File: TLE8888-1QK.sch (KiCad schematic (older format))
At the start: 38 parts, among them Q1 IPD30N06S2L-23, U2 TLE8888QK

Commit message: Update (#46)
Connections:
- net CRNK+: now also R17.2
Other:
- moved on the sheet: R17
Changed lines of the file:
@@
 L Device:R R17
 U 1 1 5C8A0B54
-P 11425 5850
-F 0 "R17" V 11475 6025 50  0000 C CNN
-F 1 "DNP" V 11425 5850 50  0000 C CNN
-F 2 "Resistor_SMD:R_0603_1608Metric_Pad1.05x0.95mm_HandSolder" V 11355 5850 50  0001 C CNN
-F 3 "~" H 11425 5850 50  0001 C CNN
-F 4 "MOUSER" H -3025 -500 50  0001 C CNN "VEND"
-	1    11425 5850
+P 13075 5900
+F 0 "R17" V 13125 6075 50  0000 C CNN
+F 1 "DNP" V 13075 5900 50  0000 C CNN
+F 2 "Resistor_SMD:R_0603_1608Metric_Pad1.05x0.95mm_HandSolder" V 13005 5900 50  0001 C CNN
+F 3 "~" H 13075 5900 50  0001 C CNN
+F 4 "MOUSER" H -1375 -450 50  0001 C CNN "VEND"
+	1    13075 5900
 	0    1    1    0
 $EndComp
@@
 Wire Wire Line
 	9750 10725 9750 11200
-Text Label 11900 11300 3    60   ~ 0
+Text Label 11900 11300 3    60   ~ 6
 VDD
-Text HLabel 11900 11200 2    60   Input ~ 0
+Text HLabel 11900 11200 2    60   Input ~ 6
 VDD
 Wire Wire Line
@@
 Wire Wire Line
 	11900 10500 11900 10800
-Text Label 12850 10300 0    60   ~ 0
+Text Label 12850 10300 0    60   ~ 6
 VDD
-Text Label 7200 10700 2    60   ~ 0
+Text Label 7200 10700 2    60   ~ 6
 VDD
 Wire Wire Line
 	7500 10700 9250 10700
-Text Label 7300 10100 2    60   ~ 0
+Text Label 7300 10100 2    60   ~ 6
 VDD
 Wire Wire Line
@@
 Connection ~ 12850 6550
 Wire Wire Line
-	11275 5900 11075 5900
-Wire Wire Line
-	11275 5900 11275 5850
+	12925 5950 12725 5950
+Wire Wire Line
+	12925 5950 12925 5900
 Wire Wire Line
 	13000 6800 13050 6800
@@
 	11150 6500 11150 6450
 Wire Wire Line
-	11075 5900 11075 6200
+	12725 5950 12725 6250
 Wire Wire Line
 	12850 6550 12850 6750
@@
 Wire Notes Line
 	14500 7000 14500 5650
-Text Notes 13750 6050 0    50   ~ 0
+Text Notes 13750 6050 0    50   ~ 6
 TRIGGER CONFIG\nAS SEEN\nAT PCB
 Text Label 13475 6800 0    60   ~ 12
@@
 Text Label 13475 6700 0    60   ~ 12
 GND
-Text Label 11575 5850 0    60   ~ 12
+Text Label 13225 5900 0    60   ~ 12
 V5V
 Text Label 13675 7150 0    60   ~ 12
@@
 	1    0    0    -1
 $EndComp
-Text Notes 13575 6450 0    50   ~ 0
+Text Notes 13575 6450 0    50   ~ 6
 SEE DATASHEET \nFOR HALL SENSOR USE
 Wire Wire Line
@@
 Connection ~ 12675 6250
 Wire Wire Line
-	12675 6250 12800 6250
+	12675 6250 12725 6250
 Connection ~ 12675 6550
 Wire Wire Line
@@
 Wire Wire Line
 	12800 6250 13175 6250
+Connection ~ 12725 6250
+Wire Wire Line
+	12725 6250 12800 6250
 $EndSCHEMATC

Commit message: Ready To Go! (#53)
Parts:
- R12, R13, R17, R18, R19, R20, R21: VEND MOUSER -> (none)
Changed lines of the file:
@@
 F 2 "Resistor_SMD:R_0603_1608Metric_Pad1.05x0.95mm_HandSolder" V 12380 6250 50  0001 C CNN
 F 3 "~" H 12450 6250 50  0001 C CNN
-F 4 "MOUSER" H -2000 -250 50  0001 C CNN "VEND"
 	1    12450 6250
 	0    1    1    0
@@
 F 2 "Resistor_SMD:R_0603_1608Metric_Pad1.05x0.95mm_HandSolder" V 12380 6550 50  0001 C CNN
 F 3 "~" H 12450 6550 50  0001 C CNN
-F 4 "MOUSER" H -2000 -250 50  0001 C CNN "VEND"
 	1    12450 6550
 	0    1    1    0
@@
 F 2 "Resistor_SMD:R_0603_1608Metric_Pad1.05x0.95mm_HandSolder" V 13005 5900 50  0001 C CNN
 F 3 "~" H 13075 5900 50  0001 C CNN
-F 4 "MOUSER" H -1375 -450 50  0001 C CNN "VEND"
 	1    13075 5900
 	0    1    1    0
@@
 F 2 "Resistor_SMD:R_0603_1608Metric_Pad1.05x0.95mm_HandSolder" V 12730 7300 50  0001 C CNN
 F 3 "~" H 12800 7300 50  0001 C CNN
-F 4 "MOUSER" H -1250 1900 50  0001 C CNN "VEND"
 	1    12800 7300
 	1    0    0    1
@@
 F 2 "Resistor_SMD:R_0603_1608Metric_Pad1.05x0.95mm_HandSolder" V 13255 7150 50  0001 C CNN
 F 3 "~" H 13325 7150 50  0001 C CNN
-F 4 "MOUSER" H -925 1900 50  0001 C CNN "VEND"
 	1    13325 7150
 	0    -1   1    0
@@
 F 2 "Resistor_SMD:R_0603_1608Metric_Pad1.05x0.95mm_HandSolder" V 13130 6700 50  0001 C CNN
 F 3 "~" H 13200 6700 50  0001 C CNN
-F 4 "MOUSER" H -1250 -250 50  0001 C CNN "VEND"
 	1    13200 6700
 	0    1    1    0
@@
 F 2 "Resistor_SMD:R_0603_1608Metric_Pad1.05x0.95mm_HandSolder" V 13130 6800 50  0001 C CNN
 F 3 "~" H 13200 6800 50  0001 C CNN
-F 4 "MOUSER" H -1250 -150 50  0001 C CNN "VEND"
 	1    13200 6800
 	0    1    1    0

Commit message: Mostly Ola's e-mailed copy, plus some of my own fixes to his almost done revision. I also did some house cleaning, with boundary edges, removed most DRC and ERC errors, etc.
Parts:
- C1, C10, C11, C12, C13, C14, C16, C3, C35, C4, C5, C6, C7, C8, C9: footprint Capacitor_SMD:C_0603_1608Metric_Pad1.05x0.95mm_HandSolder -> Capacitor_SMD:C_0603_1608Metric
- R10, R12, R13, R15, R17, R18, R19, R2, R20, R21, R22, R3, R4, R5, R6, R7, R8, R9: footprint Resistor_SMD:R_0603_1608Metric_Pad1.05x0.95mm_HandSolder -> Resistor_SMD:R_0603_1608Metric

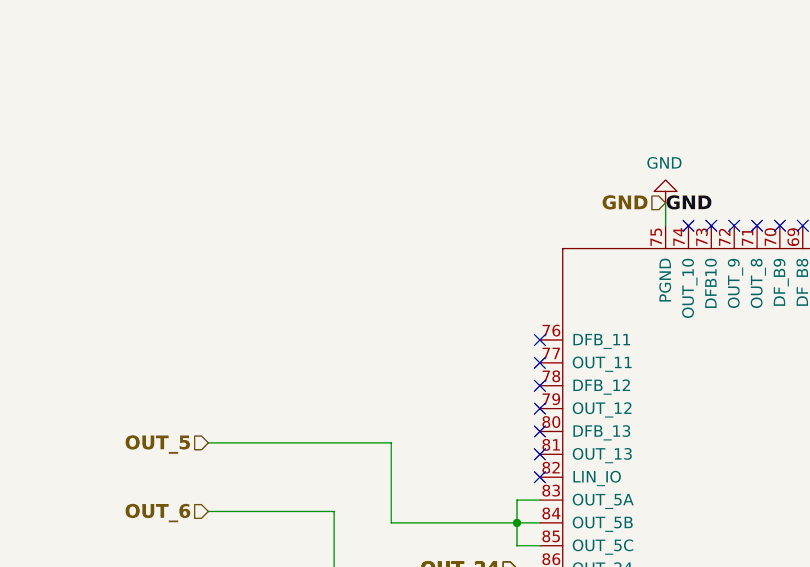
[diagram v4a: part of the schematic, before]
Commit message: added Fiducial's
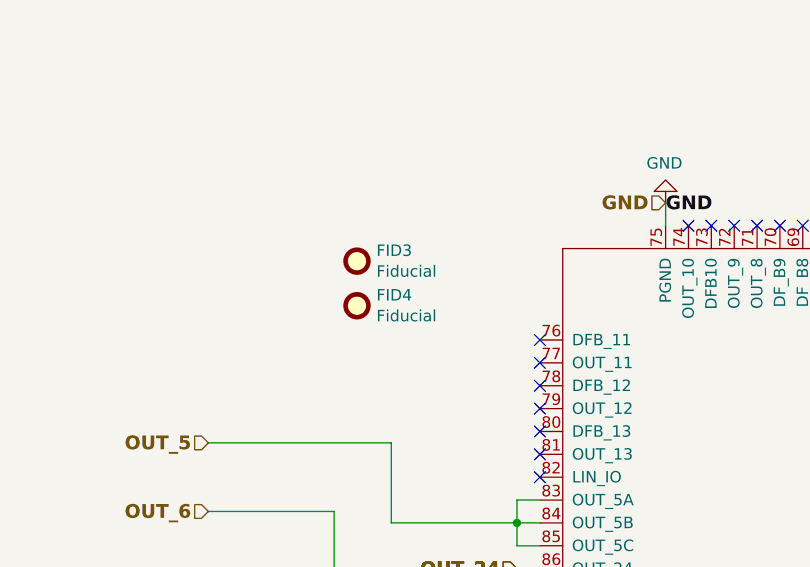
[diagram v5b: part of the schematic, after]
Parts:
- added FID3, FID4: Fiducial, Fiducial:Fiducial_0.5mm_Mask1mm, symbol Mechanical:Fiducial
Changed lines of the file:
@@
 Wire Wire Line
 	12725 6250 12800 6250
+$Comp
+L Mechanical:Fiducial FID3
+U 1 1 5D1D4069
+P 7300 6855
+F 0 "FID3" H 7385 6901 50  0000 L CNN
+F 1 "Fiducial" H 7385 6810 50  0000 L CNN
+F 2 "Fiducial:Fiducial_0.5mm_Mask1mm" H 7300 6855 50  0001 C CNN
+F 3 "~" H 7300 6855 50  0001 C CNN
+	1    7300 6855
+	1    0    0    -1
+$EndComp
+$Comp
+L Mechanical:Fiducial FID4
+U 1 1 5D1D47C2
+P 7300 7050
+F 0 "FID4" H 7385 7096 50  0000 L CNN
+F 1 "Fiducial" H 7385 7005 50  0000 L CNN
+F 2 "Fiducial:Fiducial_0.5mm_Mask1mm" H 7300 7050 50  0001 C CNN
+F 3 "~" H 7300 7050 50  0001 C CNN
+	1    7300 7050
+	1    0    0    -1
+$EndComp
 $EndSCHEMATC

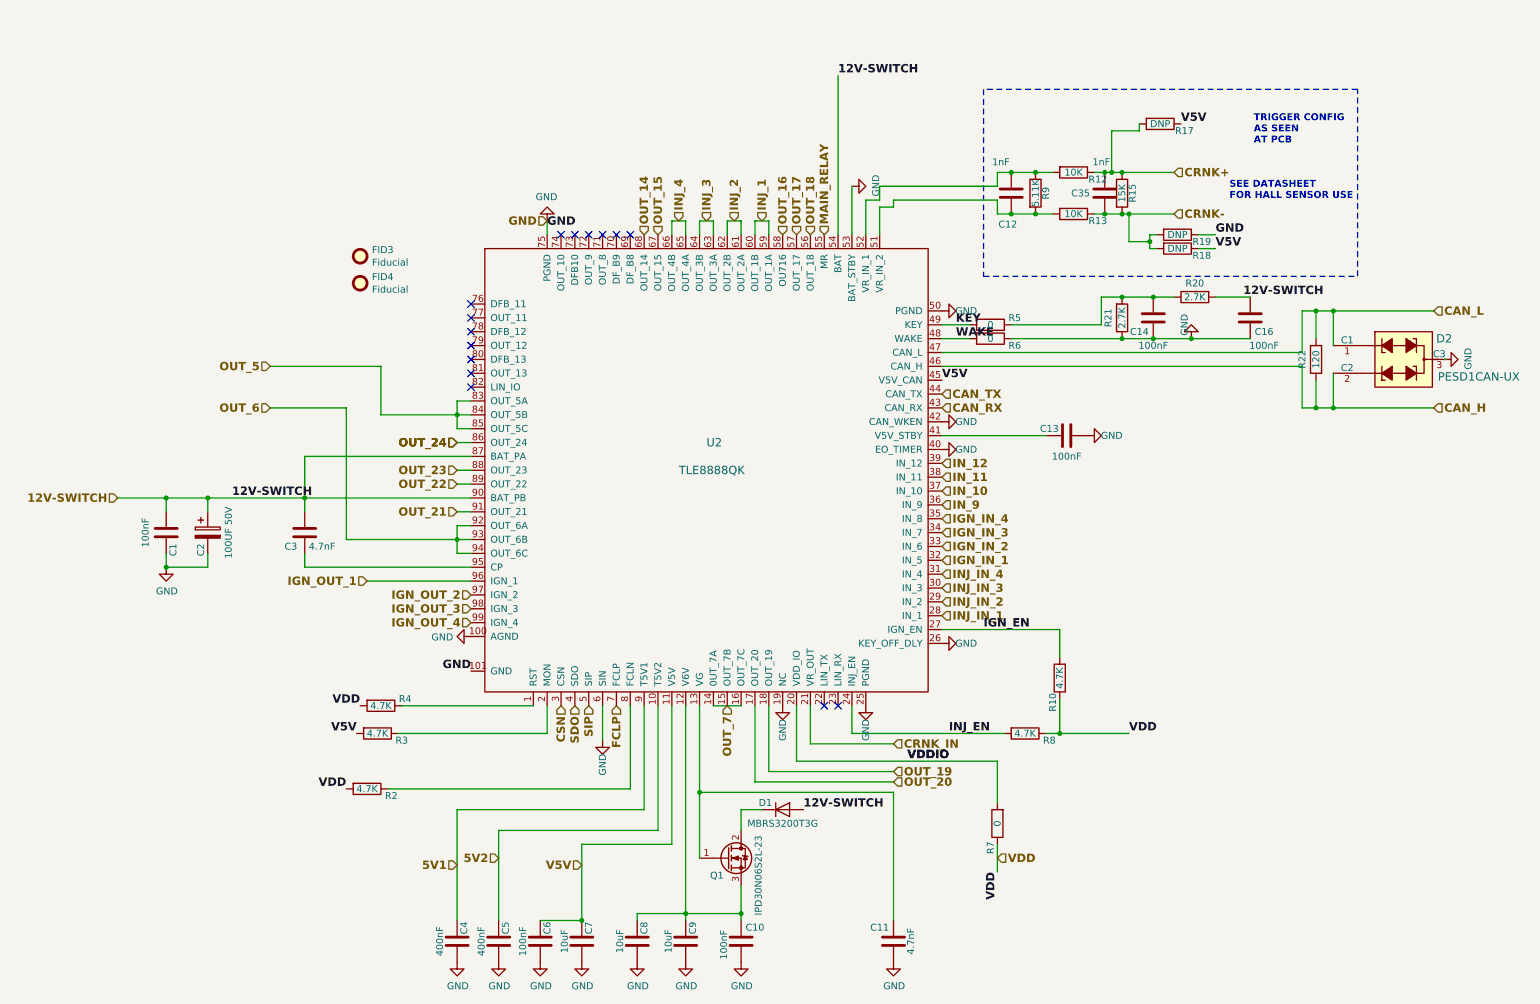
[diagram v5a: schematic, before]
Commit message: Updated logo symbol and footprint, BOM is 99% entered in KC schematic now.
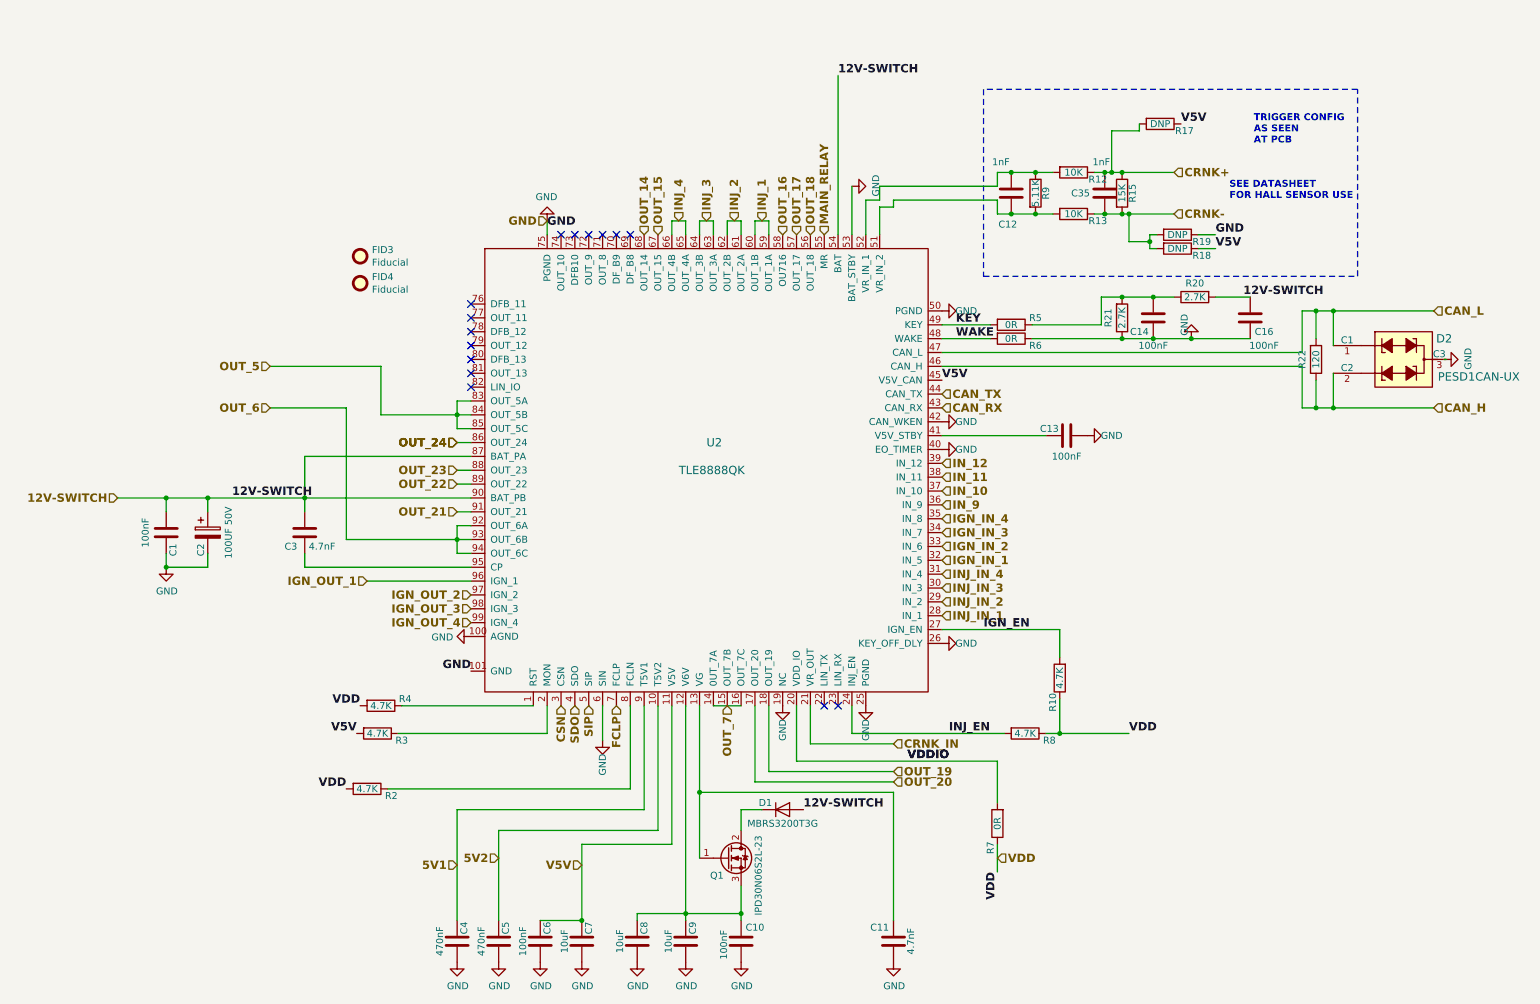
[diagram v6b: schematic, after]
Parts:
- C1, C10, C13, C14, C16, C6: Manufacturer (none) -> KEMET; Part # (none) -> C0603C104J5RACTU; VEND (none) -> DIGI; VEND# (none) -> 399-7844-1-ND
- C11, C3: Manufacturer (none) -> AVX; Part # (none) -> 06031A470JAT2A; VEND MOUSER -> DIGI; VEND# (none) -> 478-1144-1-ND
- C12, C35: Manufacturer (none) -> MURATA; Part # (none) -> GRM1885C1H102FA01D; VEND (none) -> DIGI; VEND# (none) -> 490-6377-1-ND
- C2: VEND MOUSER -> DIGI; VEND# 647-UCD1H101MNL1GS -> 493-6388-1-ND
- C4, C5: value 400nF -> 470nF; Manufacturer (none) -> TDK; Part # (none) -> CGA3E3X7R1H474K080AE; VEND (none) -> DIGI; VEND# (none) -> 445-172475-1-ND
- C7, C8, C9: Manufacturer (none) -> TDK; Part # (none) -> C1608X5R1E106M080AC; VEND (none) -> DIGI; VEND# (none) -> 445-9015-1-ND
- D1: VEND MOUSER -> DIGI; VEND# 863-MBRS3200T3G -> MBRS3200T3GOSCT-ND
- D2: Manufacturer Nexperia USA Inc. -> Nexperia; VEND MOUSER -> DIGI; VEND# 771-PESD1CANUX -> 1727-1306-1-ND
- FID3, FID4: Manufacturer (none) -> DNP; Part # (none) -> DNP; VEND (none) -> DNP; VEND# (none) -> DNP
- Q1: VEND MOUSER -> DIGI; VEND# 726-IPD30N06S2L23AT3 -> IPD30N06S2L23ATMA3CT-ND
- R10, R2, R3, R4, R8: Manufacturer (none) -> StackPole; Part # (none) -> RMCF0603JT4K70; VEND MOUSER -> DIGI; VEND# (none) -> RMCF0603JT4K70CT-ND
- R12, R13: Manufacturer (none) -> StackPole; Part # (none) -> RMCF0603JT10K0; VEND (none) -> DIGI; VEND# (none) -> RMCF0603JT10K0CT-ND
- R15: Manufacturer (none) -> StackPole; Part # (none) -> RMCF0603JG15K0; VEND MOUSER -> DIGI; VEND# (none) -> RMCF0603JG15K0CT-ND
- R17, R18, R19: Manufacturer (none) -> DNP; Part # (none) -> DNP; VEND (none) -> DIGI; VEND# (none) -> DNP
- R20, R21: Manufacturer (none) -> StackPole; Part # (none) -> RMCF0603JT2K70; VEND (none) -> DIGI; VEND# (none) -> RMCF0603JT2K70CT-ND
- R22: Manufacturer (none) -> StackPole; Part # (none) -> RMCF0603JG120R; VEND MOUSER -> DIGI; VEND# (none) -> RMCF0603JG120RCT-ND
- R5, R6, R7: value 0 -> 0R; Manufacturer (none) -> StackPole; Part # (none) -> RMCF0603ZT0R00; VEND MOUSER -> DIGI; VEND# (none) -> RMCF0603ZT0R00CT-ND
- R9: Manufacturer (none) -> mm; Part # (none) -> dd; VEND MOUSER -> DIGI; VEND# (none) -> vv
- U2: Manufacturer (none) -> Infineon; VEND MOUSER -> DIGI; VEND# 726-TLE88882QKXUMA1 -> TLE88882QKXUMA1-ND
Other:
- moved on the sheet: R5, R6

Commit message: Several U# were changed to RN# as they are resistor networks, not semiconductor chips. RN1 is now clearly a 1k. Also some U# were changed to CN#. BOM is now completely populated.
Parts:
- R9: Manufacturer mm -> StackPole; Part # dd -> RMCF0603FT5K11; VEND# vv -> RMCF0603FT5K11CT-ND
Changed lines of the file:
@@
 F 3 "~" H 12175 6400 50  0001 C CNN
 F 4 "DIGI" H -1825 -250 50  0001 C CNN "VEND"
-F 5 "dd" H 0   0   50  0001 C CNN "Part #"
-F 6 "vv" H 0   0   50  0001 C CNN "VEND#"
-F 7 "mm" H 0   0   50  0001 C CNN "Manufacturer"
+F 5 "RMCF0603FT5K11" H 0   0   50  0001 C CNN "Part #"
+F 6 "RMCF0603FT5K11CT-ND" H 0   0   50  0001 C CNN "VEND#"
+F 7 "StackPole" H 0   0   50  0001 C CNN "Manufacturer"
 	1    12175 6400
 	1    0    0    -1
